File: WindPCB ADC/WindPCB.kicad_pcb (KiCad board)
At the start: 2 copper layers, 62.5 x 56.5 mm, 37 parts, among them J6 Conn_01x04, U1 74AHC1G14, U2 MCP2562-E-SN, U3 SeeeduinoXIAO, U5 LM7805_TO220, U6 LM7808_TO220, U7 MCP3202, U8 TSR_1-2433

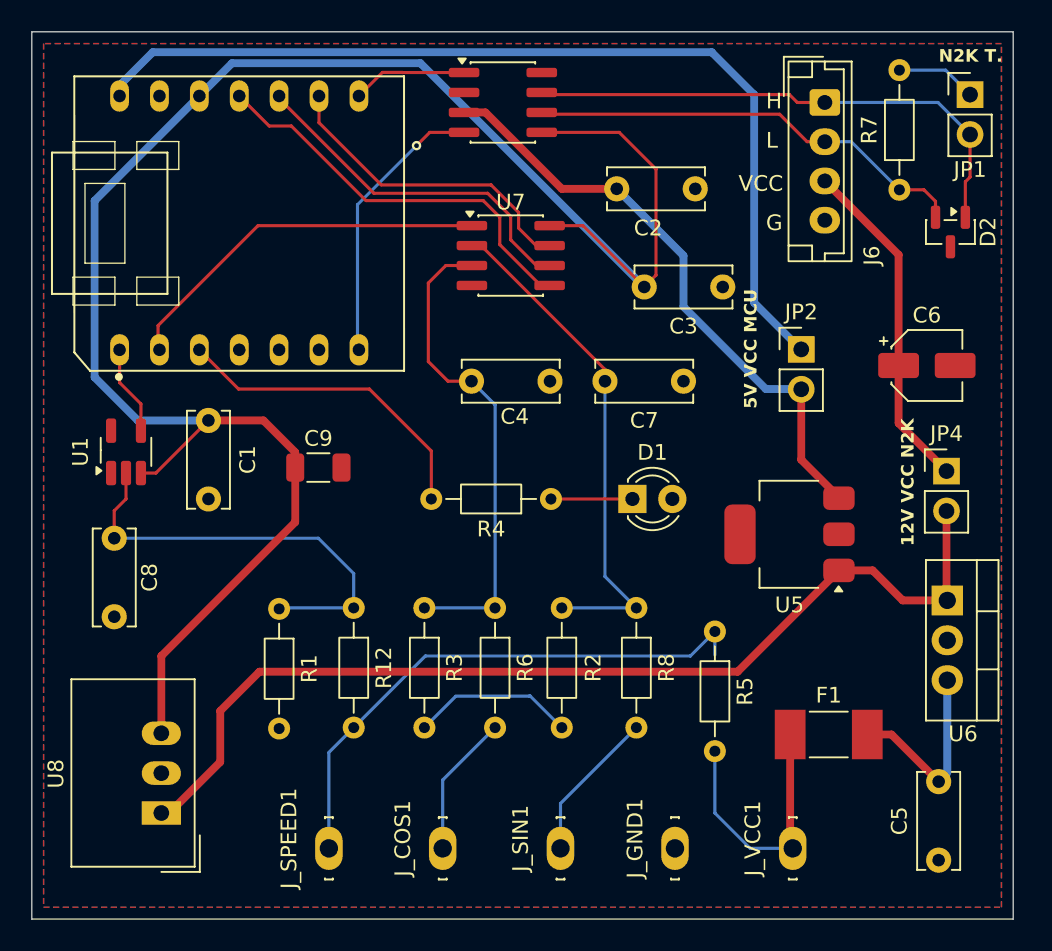
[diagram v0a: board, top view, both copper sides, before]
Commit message: Reduiced the size of the PCB (v2)
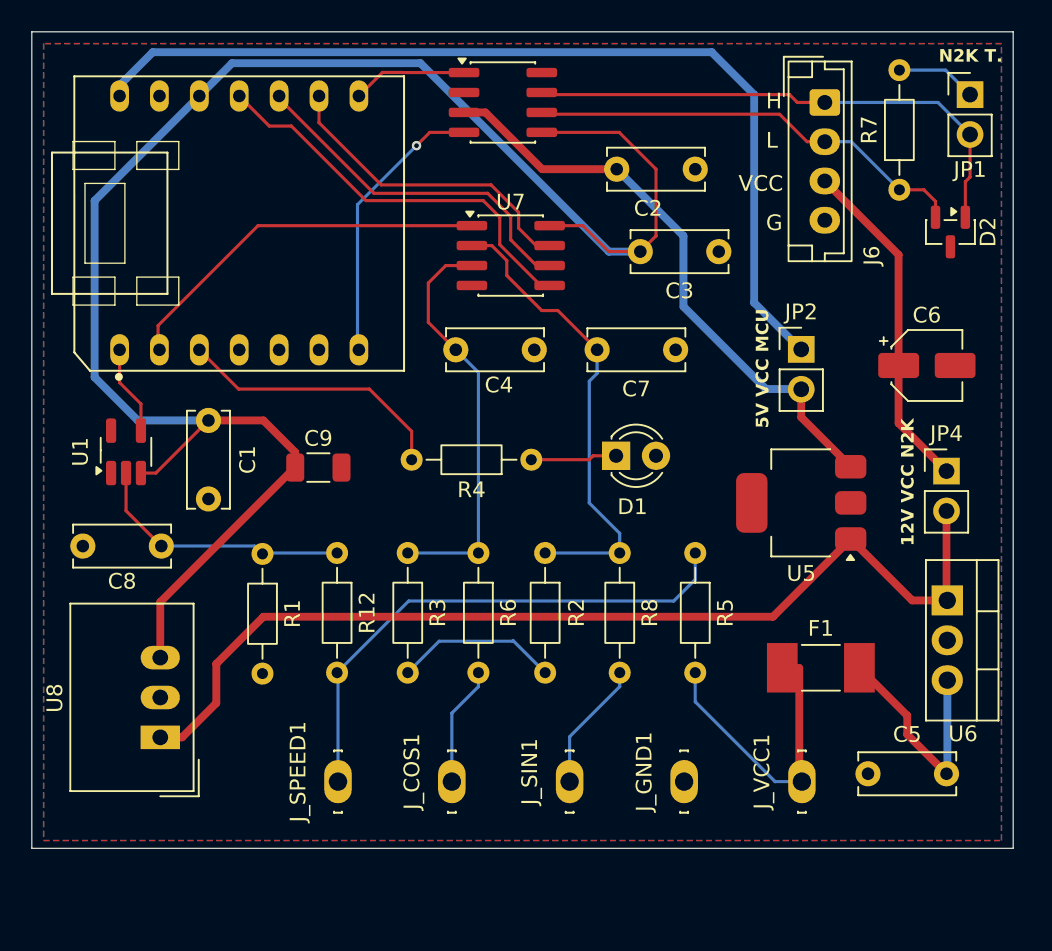
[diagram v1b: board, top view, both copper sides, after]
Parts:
- moved C5 7.11 mm to (73.0, 60.2), turned to 0 degrees
- moved R5 5.15 mm to (62.0, 46.2)
- moved U8 4.82 mm to (27.9, 57.9)
- moved J_COS1 4.29 mm to (46.5, 60.8)
- moved J_SIN1 4.29 mm to (54.0, 60.8)
- moved J_SPEED1 4.29 mm to (39.2, 60.8)
- moved J_GND1 4.29 mm to (61.3, 60.8)
- moved J_VCC1 4.29 mm to (68.8, 60.8)
- moved F1 4.28 mm to (70.0, 53.5)
- moved R1 3.66 mm to (34.4, 46.2)
- moved R12 3.66 mm to (39.2, 46.2)
- moved R2 3.66 mm to (52.4, 46.2)
- moved R3 3.66 mm to (43.7, 46.2)
- moved R6 3.66 mm to (48.2, 46.2)
- moved R8 3.66 mm to (57.2, 46.2)
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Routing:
- net Net-(C8-Pad1): track 27.9 -> 17.3 mm
- net +3.3V: track 121.3 -> 112.1 mm
- net Net-(U7-CH1): track 31.3 -> 26.5 mm
- net Net-(U3-PA10_A2_D2): track 20.6 -> 17.6 mm
- net Net-(U6-VO): track 12.5 -> 15.0 mm
- net Net-(U7-CH0): track 32.5 -> 30.7 mm
- net Net-(J_SPEED1-Pad1): track 35.6 -> 33.9 mm
- net Net-(J_SIN1-Pad1): track 9.88 -> 8.45 mm
- net Net-(J_COS1-Pad1): track 9.13 -> 7.70 mm
- net +5V: track 38.6 -> 37.7 mm
- net +8V: track 17.2 -> 18.1 mm
- net +12V: track 65.2 -> 64.4 mm
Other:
- board size 62.5 x 56.5 mm -> 62.5 x 52 mm
